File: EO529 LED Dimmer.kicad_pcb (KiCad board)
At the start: 2 copper layers, 76.2 x 45.7 mm, 47 parts, among them J1 VBat, Q1 BC639, Q2 BC639, Q3 BC639, Q4 BC639, U1 NE556, U2 NE556

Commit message: Revision to circuit
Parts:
- removed D10: LED_RGBA, LED_THT:LED_BL-FL7680RGB
- removed D3, D4, D6, D7, D8, D9: 1N4148, Diode_THT:D_DO-35_SOD27_P7.62mm_Horizontal
- removed D5: White, LED_THT:LED_D10.0mm
- added R13: 10k, Resistor_THT:R_Axial_DIN0207_L6.3mm_D2.5mm_P7.62mm_Horizontal, F.Cu at (118.1, 113.0)
- added R14: 10k, Resistor_THT:R_Axial_DIN0207_L6.3mm_D2.5mm_P7.62mm_Horizontal, F.Cu at (118.1, 101.6)
- added R15: 100k, Resistor_THT:R_Axial_DIN0207_L6.3mm_D2.5mm_P7.62mm_Horizontal, F.Cu at (125.7, 116.2)
- added R16: 100k, Resistor_THT:R_Axial_DIN0207_L6.3mm_D2.5mm_P7.62mm_Horizontal, F.Cu at (128.3, 116.2)
- added R17: 1k, Resistor_THT:R_Axial_DIN0207_L6.3mm_D2.5mm_P7.62mm_Horizontal, F.Cu at (133.3, 101.6)
- added R18: 180, Resistor_THT:R_Axial_DIN0207_L6.3mm_D2.5mm_P7.62mm_Horizontal, F.Cu at (137.2, 101.6)
- added R19: 10k, Resistor_THT:R_Axial_DIN0207_L6.3mm_D2.5mm_P7.62mm_Horizontal, F.Cu at (95.9, 106.0)
- added R20: 10k, Resistor_THT:R_Axial_DIN0207_L6.3mm_D2.5mm_P7.62mm_Horizontal, F.Cu at (88.3, 102.2)
- added R21: 100k, Resistor_THT:R_Axial_DIN0207_L6.3mm_D2.5mm_P7.62mm_Horizontal, F.Cu at (95.9, 109.9)
- added R22: 100k, Resistor_THT:R_Axial_DIN0207_L6.3mm_D2.5mm_P7.62mm_Horizontal, F.Cu at (73.7, 111.8)
- added R23: 1k, Resistor_THT:R_Axial_DIN0207_L6.3mm_D2.5mm_P7.62mm_Horizontal, F.Cu at (69.8, 101.6)
- added R24: 150, Resistor_THT:R_Axial_DIN0207_L6.3mm_D2.5mm_P7.62mm_Horizontal, F.Cu at (73.7, 101.6)
- added U3: LM393, Package_DIP:DIP-8_W7.62mm_Socket, F.Cu at (77.5, 98.4)
- added U4: LM393, Package_DIP:DIP-8_W7.62mm_Socket, F.Cu at (129.5, 90.8)
- D1: value 1N4148 -> White; footprint Diode_THT:D_DO-35_SOD27_P7.62mm_Horizontal -> LED_THT:LED_D10.0mm
- D2: value 1N4148 -> LED_RGBA; footprint Diode_THT:D_DO-35_SOD27_P7.62mm_Horizontal -> LED_THT:LED_BL-FL7680RGB
- R1, R2, R7, R8: value 1k -> 10k
- R10, R3, R4, R9: value 1k -> 100k
- R12: value 1k -> 220
- R5: value 180 -> 1k
- R6: value 10k -> 220
- moved R11 112.5 mm to (133.3, 87.6), turned to 90 degrees
- moved D1 109.2 mm to (110.5, 116.8), turned to 90 degrees
- moved RV4 94.2 mm to (83.8, 112.2), turned to 90 degrees
- moved RV3 90.8 mm to (128.2, 112.2), turned to 90 degrees
- moved D2 90.4 mm to (97.8, 114.9), turned to 0 degrees
- moved R12 87.4 mm to (137.2, 87.6), turned to 90 degrees
- moved Q3 86.6 mm to (137.2, 97.2), turned to 180 degrees
- moved C6 84.3 mm to (111.8, 94.0), turned to 0 degrees
- moved J1 83.0 mm to (88.9, 118.1), turned to 180 degrees
- moved R7 82.7 mm to (111.1, 75.6)
- moved U2 77.3 mm to (107.3, 106.0)
- moved Q2 76.6 mm to (134.6, 92.1), turned to 0 degrees
- moved C8 76.6 mm to (95.2, 94.0)
- moved C5 76.4 mm to (111.8, 97.8)
- moved C9 74.3 mm to (80.6, 116.2), turned to 270 degrees
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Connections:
- D1 pad 2: Net-(D1-Pad2) -> VCC
- D2 pad 1: Net-(D1-Pad2) -> Red
- D2 pad 2: Net-(D2-Pad2) -> Green
- R1 pad 1: Net-(Q1-Pad3) -> VCC
- R10 pad 1: Net-(Q2-Pad2) -> Net-(R10-Pad1)
- R10 pad 2: Net-(D5-Pad1) -> GND
- R11 pad 1: Net-(Q4-Pad2) -> Net-(Q2-Pad3)
- R11 pad 2: Green -> Net-(R11-Pad2)
- R12 pad 1: Net-(Q3-Pad2) -> Net-(Q2-Pad2)
- R2 pad 1: Net-(Q2-Pad3) -> Net-(R1-Pad2)
- R2 pad 2: Net-(R2-Pad2) -> Net-(C2-Pad1)
- R3 pad 2: Net-(D1-Pad2) -> Net-(R3-Pad2)
- R4 pad 1: VCC -> Net-(R4-Pad1)
- R4 pad 2: Net-(D3-Pad2) -> GND
- R5 pad 1: Net-(Q1-Pad2) -> Net-(Q1-Pad3)
- R5 pad 2: Red -> Net-(R5-Pad2)
- R6 pad 1: Net-(Q3-Pad3) -> Net-(Q1-Pad2)
- R6 pad 2: Net-(R6-Pad2) -> Green
- R7 pad 1: Net-(Q4-Pad3) -> VCC
- R8 pad 1: VCC -> Net-(R7-Pad2)
- R8 pad 2: Net-(D6-Pad2) -> Net-(C4-Pad1)
- R9 pad 2: Net-(D8-Pad2) -> Net-(R9-Pad2)
- RV1 pad 1: Net-(D1-Pad1) -> Net-(R4-Pad1)
- RV1 pad 2: Net-(C3-Pad1) -> Net-(RV1-Pad2)
- RV1 pad 3: Net-(D2-Pad2) -> Net-(R3-Pad2)
- RV2 pad 1: Net-(D3-Pad1) -> Net-(R10-Pad1)
- RV2 pad 2: Net-(C4-Pad1) -> Net-(RV2-Pad2)
- RV2 pad 3: Net-(D4-Pad2) -> Net-(R9-Pad2)
- RV3 pad 2: Net-(C7-Pad1) -> Net-(RV3-Pad2)
- RV4 pad 2: Net-(C8-Pad1) -> Net-(RV4-Pad2)
- U1 pad 1: Net-(D1-Pad2) -> Net-(R1-Pad2)
- U1 pad 11: Net-(C2-Pad1) -> Net-(C3-Pad1)
- U1 pad 13: Net-(D3-Pad2) -> Net-(R7-Pad2)
- U1 pad 2: Net-(C3-Pad1) -> Net-(C2-Pad1)
- U1 pad 5: Net-(R1-Pad2) -> Net-(U1-Pad5)
- U1 pad 6: Net-(C3-Pad1) -> Net-(C2-Pad1)
- U1 pad 9: Net-(R2-Pad2) -> Net-(U1-Pad9)
- U2 pad 1: Net-(D6-Pad2) -> Net-(R13-Pad2)
- U2 pad 11: Net-(C6-Pad1) -> Net-(C7-Pad1)
- U2 pad 13: Net-(D8-Pad2) -> Net-(R19-Pad2)
- U2 pad 2: Net-(C7-Pad1) -> Net-(C6-Pad1)
- U2 pad 5: Net-(R6-Pad2) -> Net-(U2-Pad5)
- U2 pad 6: Net-(C7-Pad1) -> Net-(C6-Pad1)
- U2 pad 9: Net-(R7-Pad2) -> Net-(U2-Pad9)
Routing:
- net GND: track 210.0 -> 285.7 mm
- net VCC: track 119.5 -> 194.7 mm
- net Net-(C2-Pad1): track 3.91 -> 44.1 mm
- net Red: track 65.9 -> 27.5 mm
- net Net-(C7-Pad1): track 40.2 -> 4.71 mm
- net Net-(D5-Pad1): track 32.6 -> 0.00 mm
- net Blue: track 44.4 -> 75.9 mm
- net Net-(C3-Pad1): track 37.2 -> 8.83 mm
- net Net-(C6-Pad1): track 3.91 -> 31.2 mm
- net Net-(D6-Pad2): track 24.0 -> 0.00 mm
- net Net-(D1-Pad2): track 23.6 -> 0.00 mm
- net Net-(D3-Pad2): track 23.2 -> 0.00 mm
- net Net-(D8-Pad2): track 22.6 -> 0.00 mm
- net Net-(R17-Pad2): track 0.00 -> 17.6 mm
- net Net-(D1-Pad1): track 14.0 -> 31.3 mm
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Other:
- board size 76.2 x 45.7 mm -> 77.5 x 52.7 mm
- board text added: "- +"
- board text removed: "+ -"
- board text removed: "PWM LED Controller Board EO529 Part A"
- board text removed: "University of Brighton EEE V1.0 Aria Tso 21839447"

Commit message: Updated working design
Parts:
- added R25: 1M, Resistor_THT:R_Axial_DIN0207_L6.3mm_D2.5mm_P7.62mm_Horizontal, F.Cu at (92.1, 79.4)
- added R26: 1M, Resistor_THT:R_Axial_DIN0207_L6.3mm_D2.5mm_P7.62mm_Horizontal, F.Cu at (114.9, 106.1)
- added R27: 1M, Resistor_THT:R_Axial_DIN0207_L6.3mm_D2.5mm_P7.62mm_Horizontal, F.Cu at (130.8, 71.8)
- added R28: 1M, Resistor_THT:R_Axial_DIN0207_L6.3mm_D2.5mm_P7.62mm_Horizontal, F.Cu at (76.2, 113.7)
- added TP1: TestPoint, TestPoint:TestPoint_THTPad_D2.0mm_Drill1.0mm, F.Cu at (101.0, 117.5)
- added TP2: TestPoint, TestPoint:TestPoint_THTPad_D2.0mm_Drill1.0mm, F.Cu at (101.0, 113.1)
- R10, R15, R16, R21, R22, R3, R4, R9: value 100k -> 82k
- R24: value 150 -> 180
- R6: value 220 -> 150
- moved J1 33.6 mm to (122.4, 118.8), turned to -90 degrees
- moved C9 30.6 mm to (111.1, 118.9)
- moved C10 22.6 mm to (116.2, 117.6)
- moved D1 18.3 mm to (93.3, 123.3)
- moved R22 16.5 mm to (87.6, 102.9), turned to 90 degrees
- moved D2 11.3 mm to (101.1, 125.7), turned to 90 degrees
- moved R10 9.31 mm to (119.4, 82.6), turned to -90 degrees
- moved R15 8.01 mm to (118.1, 113.7), turned to 0 degrees
- moved R13 7.02 mm to (111.1, 113.7)
- moved H2 5.78 mm to (67.3, 125.2)
- moved H4 5.78 mm to (139.7, 125.2)
- moved R5 5.46 mm to (72.4, 85.3), turned to 90 degrees
- moved R24 5.22 mm to (68.6, 100.4)
- moved R19 3.93 mm to (95.2, 109.9)
- moved R20 3.93 mm to (87.6, 106.1)
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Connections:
- D1 pad 1: Net-(D1-Pad1) -> Net-(R24-Pad2)
- D1 pad 2: VCC -> V_LED
- D2 pad 4: VCC -> V_LED
- R12 pad 2: Blue -> Green
- R18 pad 2: Net-(D1-Pad1) -> Blue
- R24 pad 2: Red -> Net-(R24-Pad2)
- R6 pad 2: Green -> Red
- U1 pad 5: Net-(U1-Pad5) -> unconnected-(U1-Pad5)
- U1 pad 9: Net-(U1-Pad9) -> unconnected-(U1-Pad9)
- U2 pad 5: Net-(U2-Pad5) -> unconnected-(U2-Pad5)
- U2 pad 9: Net-(U2-Pad9) -> unconnected-(U2-Pad9)
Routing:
- net GND: track 285.7 -> 29.2 mm
- net Red: track 27.5 -> 74.8 mm
- net Net-(R24-Pad2): track 0.00 -> 32.6 mm
- net Net-(D1-Pad1): track 31.3 -> 0.00 mm
- net Blue: track 75.9 -> 45.4 mm
- net Net-(U3-Pad7): track 9.96 -> 39.8 mm
- net Net-(U4-Pad7): track 17.6 -> 39.2 mm
- net V_LED: track 0.00 -> 10.9 mm
- net VCC: track 194.7 -> 204.5 mm
- net Net-(Q1-Pad3): track 13.4 -> 5.17 mm
- net Net-(R11-Pad2): track 12.4 -> 20.3 mm
- net Net-(Q4-Pad3): track 5.11 -> 12.8 mm
- net Net-(C2-Pad1): track 44.1 -> 36.6 mm
- net Green: track 70.1 -> 77.4 mm
- net Net-(R23-Pad2): track 14.0 -> 20.0 mm
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- added copper zone on B.Cu, net GND
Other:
- board size 77.5 x 52.7 mm -> 77.5 x 58.4 mm
- net class Default removed
- rule pad_to_mask_clearance: 0.05 -> 0
- board text added: "VCC Bridge"

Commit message: Final revision
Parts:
- removed H1, H2, H3, H4: MountingHole, MountingHole:MountingHole_2.2mm_M2
- removed the R11 at (134.6, 85.4)
- removed the R17 at (134.6, 100.4)
- removed the R23 at (72.4, 100.4)
- removed the R5 at (72.4, 85.3)
- R11: renamed from R27; value 1M -> 4.7k
- R12: value 220 -> 180; footprint Resistor_THT:R_Axial_DIN0207_L6.3mm_D2.5mm_P7.62mm_Horizontal -> Resistor_THT:R_Axial_DIN0414_L11.9mm_D4.5mm_P15.24mm_Horizontal
- R17: renamed from R26; value 1M -> 4.7k
- R18, R6: footprint Resistor_THT:R_Axial_DIN0207_L6.3mm_D2.5mm_P7.62mm_Horizontal -> Resistor_THT:R_Axial_DIN0414_L11.9mm_D4.5mm_P15.24mm_Horizontal
- R23: renamed from R28; value 1M -> 4.7k
- R24: value 180 -> 220; footprint Resistor_THT:R_Axial_DIN0207_L6.3mm_D2.5mm_P7.62mm_Horizontal -> Resistor_THT:R_Axial_DIN0414_L11.9mm_D4.5mm_P15.24mm_Horizontal
- R5: renamed from R25; value 1M -> 4.7k
- moved TP2 11.1 mm to (111.1, 117.5)
- moved C9 8.89 mm to (120.0, 118.9)
- moved R16 6.40 mm to (121.9, 114.4)
- moved R4 6.37 mm to (85.1, 72.5)
- moved J1 4.60 mm to (127.0, 119.4)
- moved R6 3.88 mm to (71.8, 87.5)
- moved R12 3.66 mm to (135.3, 87.2)
- moved R24 3.36 mm to (71.8, 101.5)
- moved R18 3.25 mm to (135.3, 101.1)
- moved Q1 2.93 mm to (70.5, 92.2)
- moved Q2 2.63 mm to (134.0, 91.8)
- moved Q4 2.21 mm to (73.0, 96.7)
- moved Q3 2.03 mm to (136.5, 96.3)
- moved C10 1.27 mm to (114.9, 117.6)
- moved R3 0.90 mm to (88.3, 72.5), turned to -90 degrees
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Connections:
- R11 pad 1: Net-(R11-Pad2) -> Net-(Q2-Pad3)
- R17 pad 1: Net-(U4-Pad7) -> Net-(Q3-Pad3)
- R23 pad 1: Net-(R23-Pad2) -> Net-(Q4-Pad3)
- R5 pad 1: Net-(U3-Pad7) -> Net-(Q1-Pad3)
- U3 pad 1: Net-(R23-Pad2) -> Net-(Q4-Pad3)
- U3 pad 2: Net-(C8-Pad1) -> Net-(RV4-Pad2)
- U3 pad 3: Net-(RV4-Pad2) -> Net-(C8-Pad1)
- U3 pad 5: Net-(RV1-Pad2) -> Net-(C2-Pad1)
- U3 pad 6: Net-(C2-Pad1) -> Net-(RV1-Pad2)
- U3 pad 7: Net-(U3-Pad7) -> Net-(Q1-Pad3)
- U4 pad 1: Net-(R11-Pad2) -> Net-(Q2-Pad3)
- U4 pad 2: Net-(C4-Pad1) -> Net-(RV2-Pad2)
- U4 pad 3: Net-(RV2-Pad2) -> Net-(C4-Pad1)
- U4 pad 5: Net-(RV3-Pad2) -> Net-(C6-Pad1)
- U4 pad 6: Net-(C6-Pad1) -> Net-(RV3-Pad2)
- U4 pad 7: Net-(U4-Pad7) -> Net-(Q3-Pad3)
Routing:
- net Net-(U3-Pad7): track 39.8 -> 0.00 mm
- net Net-(U4-Pad7): track 39.2 -> 0.00 mm
- net Net-(Q1-Pad3): track 5.17 -> 27.7 mm
- net Net-(Q3-Pad3): track 5.29 -> 27.7 mm
- net Net-(R11-Pad2): track 20.3 -> 0.00 mm
- net Net-(R23-Pad2): track 20.0 -> 0.00 mm
- net Net-(Q2-Pad3): track 12.6 -> 30.1 mm
- net Net-(Q4-Pad3): track 12.8 -> 29.9 mm
- net VCC: track 204.5 -> 215.4 mm
- net Blue: track 45.4 -> 35.9 mm
- net Net-(D1-Pad1): track 32.6 -> 24.3 mm
- net Red: track 74.8 -> 82.6 mm
- net GND: track 29.2 -> 21.5 mm
- net Net-(C4-Pad1): track 42.8 -> 35.7 mm
- net Net-(C8-Pad1): track 42.4 -> 36.3 mm
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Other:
- board size 77.5 x 58.4 mm -> 73.7 x 58.4 mm
- board text added: "-Bridge-"
- board text removed: "VCC Bridge"

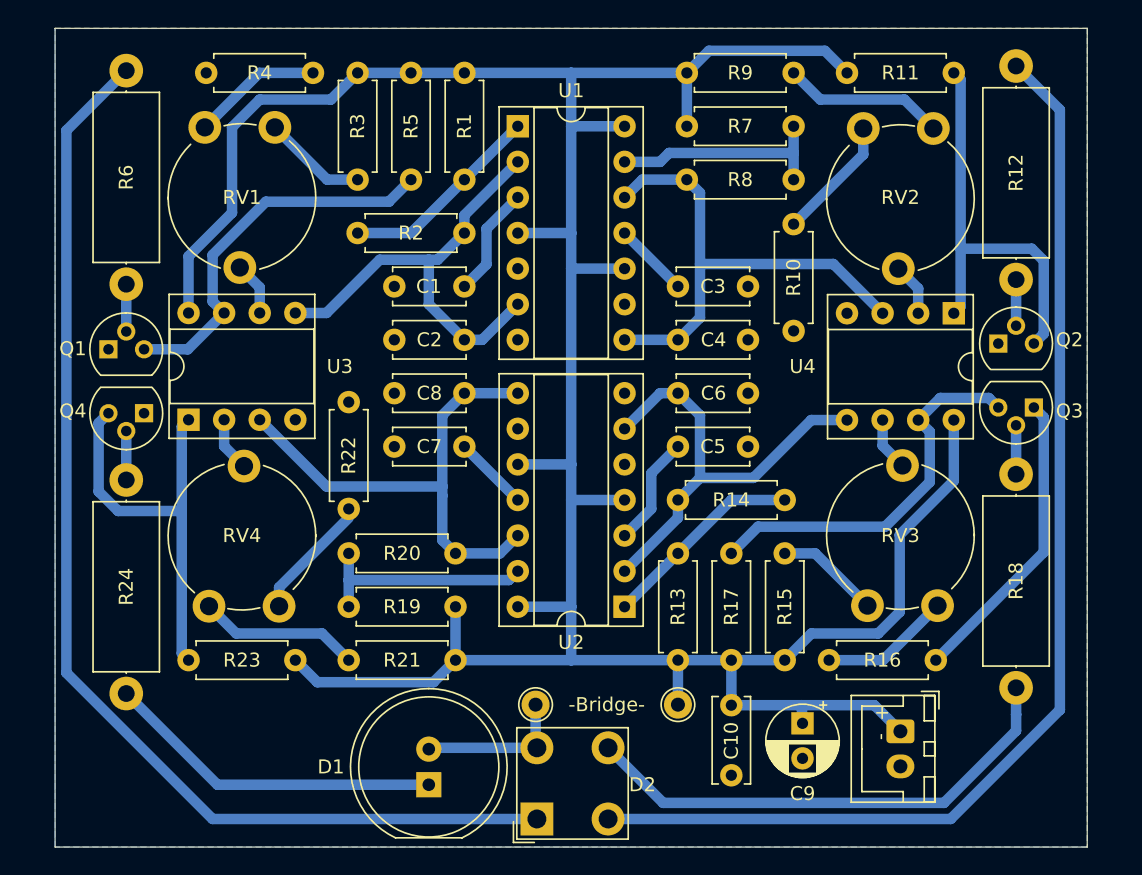
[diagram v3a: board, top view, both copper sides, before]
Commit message: Revert "Final revision"
This reverts commit 9e4e9cd728e1364b963bc449a0773ff88f127e0e.
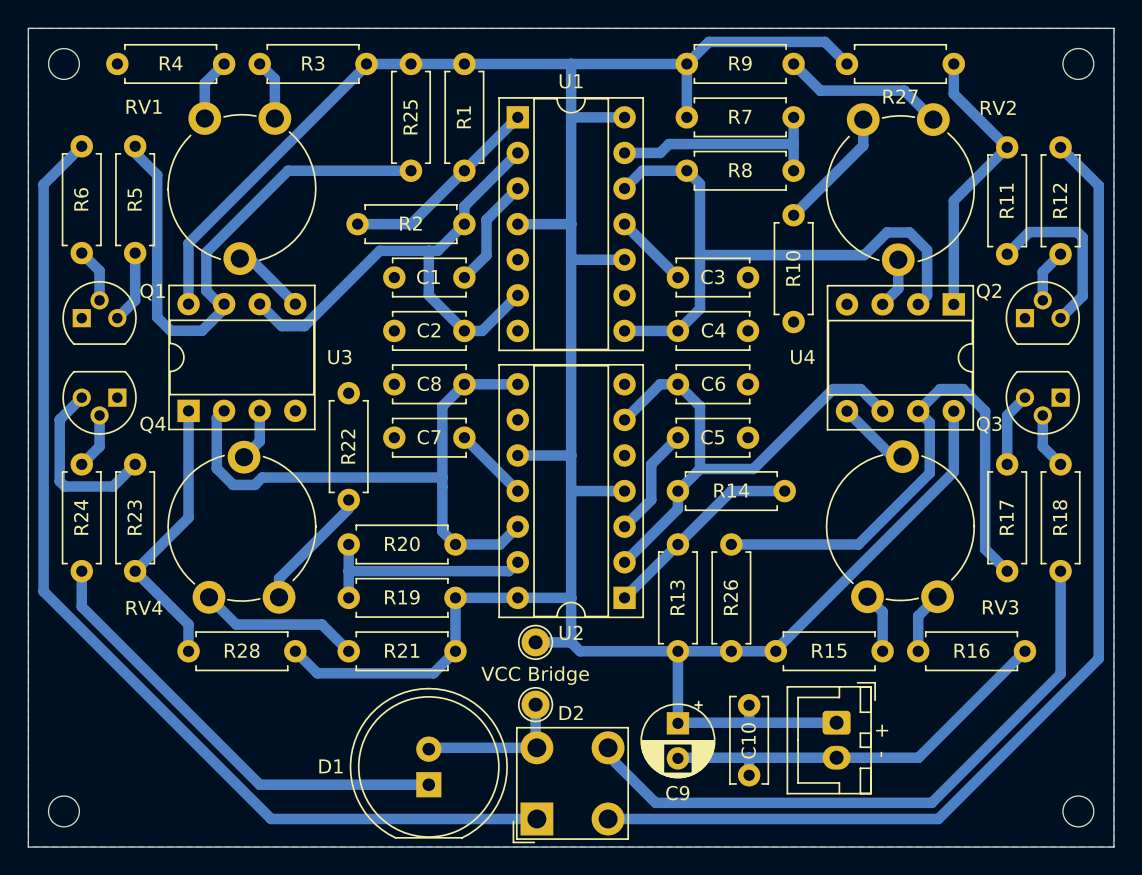
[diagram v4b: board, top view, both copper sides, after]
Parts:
- added H1: MountingHole, MountingHole:MountingHole_2.2mm_M2, F.Cu at (67.3, 71.8)
- added H2: MountingHole, MountingHole:MountingHole_2.2mm_M2, F.Cu at (67.3, 125.2)
- added H3: MountingHole, MountingHole:MountingHole_2.2mm_M2, F.Cu at (139.7, 71.8)
- added H4: MountingHole, MountingHole:MountingHole_2.2mm_M2, F.Cu at (139.7, 125.2)
- added R11: 1k, Resistor_THT:R_Axial_DIN0207_L6.3mm_D2.5mm_P7.62mm_Horizontal, F.Cu at (134.6, 85.4)
- added R17: 1k, Resistor_THT:R_Axial_DIN0207_L6.3mm_D2.5mm_P7.62mm_Horizontal, F.Cu at (134.6, 100.4)
- added R23: 1k, Resistor_THT:R_Axial_DIN0207_L6.3mm_D2.5mm_P7.62mm_Horizontal, F.Cu at (72.4, 100.4)
- added R5: 1k, Resistor_THT:R_Axial_DIN0207_L6.3mm_D2.5mm_P7.62mm_Horizontal, F.Cu at (72.4, 85.3)
- R12: value 180 -> 220; footprint Resistor_THT:R_Axial_DIN0414_L11.9mm_D4.5mm_P15.24mm_Horizontal -> Resistor_THT:R_Axial_DIN0207_L6.3mm_D2.5mm_P7.62mm_Horizontal
- R18, R6: footprint Resistor_THT:R_Axial_DIN0414_L11.9mm_D4.5mm_P15.24mm_Horizontal -> Resistor_THT:R_Axial_DIN0207_L6.3mm_D2.5mm_P7.62mm_Horizontal
- R24: value 220 -> 180; footprint Resistor_THT:R_Axial_DIN0414_L11.9mm_D4.5mm_P15.24mm_Horizontal -> Resistor_THT:R_Axial_DIN0207_L6.3mm_D2.5mm_P7.62mm_Horizontal
- R25: renamed from R5; value 4.7k -> 1M
- R26: renamed from R17; value 4.7k -> 1M
- R27: renamed from R11; value 4.7k -> 1M
- R28: renamed from R23; value 4.7k -> 1M
- moved TP2 11.1 mm to (101.0, 113.1)
- moved C9 8.89 mm to (111.1, 118.9)
- moved R16 6.40 mm to (128.3, 113.7)
- moved R4 6.37 mm to (78.7, 71.8)
- moved J1 4.60 mm to (122.4, 118.8)
- moved R6 3.88 mm to (68.6, 85.3)
- moved R12 3.66 mm to (138.4, 85.4)
- moved R24 3.36 mm to (68.6, 100.4)
- moved R18 3.25 mm to (138.4, 100.4)
- moved Q1 2.93 mm to (68.6, 90.0)
- moved Q2 2.63 mm to (135.9, 90.0)
- moved Q4 2.21 mm to (71.1, 95.6)
- moved Q3 2.03 mm to (138.4, 95.6)
- moved C10 1.27 mm to (116.2, 117.6)
- moved R3 0.90 mm to (88.9, 71.8), turned to 180 degrees
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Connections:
- R25 pad 1: Net-(Q1-Pad3) -> Net-(U3-Pad7)
- R26 pad 1: Net-(Q3-Pad3) -> Net-(U4-Pad7)
- R27 pad 1: Net-(Q2-Pad3) -> Net-(R11-Pad2)
- R28 pad 1: Net-(Q4-Pad3) -> Net-(R23-Pad2)
- U3 pad 1: Net-(Q4-Pad3) -> Net-(R23-Pad2)
- U3 pad 2: Net-(RV4-Pad2) -> Net-(C8-Pad1)
- U3 pad 3: Net-(C8-Pad1) -> Net-(RV4-Pad2)
- U3 pad 5: Net-(C2-Pad1) -> Net-(RV1-Pad2)
- U3 pad 6: Net-(RV1-Pad2) -> Net-(C2-Pad1)
- U3 pad 7: Net-(Q1-Pad3) -> Net-(U3-Pad7)
- U4 pad 1: Net-(Q2-Pad3) -> Net-(R11-Pad2)
- U4 pad 2: Net-(RV2-Pad2) -> Net-(C4-Pad1)
- U4 pad 3: Net-(C4-Pad1) -> Net-(RV2-Pad2)
- U4 pad 5: Net-(C6-Pad1) -> Net-(RV3-Pad2)
- U4 pad 6: Net-(RV3-Pad2) -> Net-(C6-Pad1)
- U4 pad 7: Net-(Q3-Pad3) -> Net-(U4-Pad7)
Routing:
- net Net-(U3-Pad7): track 0.00 -> 39.8 mm
- net Net-(U4-Pad7): track 0.00 -> 39.2 mm
- net Net-(Q1-Pad3): track 27.7 -> 5.17 mm
- net Net-(Q3-Pad3): track 27.7 -> 5.29 mm
- net Net-(R11-Pad2): track 0.00 -> 20.3 mm
- net Net-(R23-Pad2): track 0.00 -> 20.0 mm
- net Net-(Q2-Pad3): track 30.1 -> 12.6 mm
- net Net-(Q4-Pad3): track 29.9 -> 12.8 mm
- net VCC: track 215.4 -> 204.5 mm
- net Blue: track 35.9 -> 45.4 mm
- net Net-(R24-Pad2): track 24.3 -> 32.6 mm
- net Red: track 82.6 -> 74.8 mm
- net GND: track 21.5 -> 29.2 mm
- net Net-(C4-Pad1): track 35.7 -> 42.8 mm
- net Net-(C8-Pad1): track 36.3 -> 42.4 mm
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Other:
- board size 73.7 x 58.4 mm -> 77.5 x 58.4 mm
- board text added: "VCC Bridge"
- board text removed: "-Bridge-"
